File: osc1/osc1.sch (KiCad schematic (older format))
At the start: 48 parts

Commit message: Continued work on OSC1
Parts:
- added C?: 0.1u, symbol Device:C
- added C?: 10n, symbol Device:C
- added J?: Lin FM, symbol Connector:AudioJack2
- added R?: 1M, symbol Device:R
- added R?: 470, symbol Device:R
- added R? (x3): ?, symbol Device:R
- added RV? (x2): ?, symbol Device:R_POT
- R?: value 24k -> 100k
- RV?: value 10k -> 20k
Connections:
- net 1VOctave is gone; now on an unnamed net: R?.1
- net HIGHFREQTRACK is gone; now on net GND: RV?.3
- net +12V: now also R?.2, RV?.1, RV?.1
- net -12V: no longer J?.S
- net GND: now also J?.S, C?.1, J?.S, R?.1, R?.1
- net LINFM: now reaches U?.13 (VLFI)
- net LINFM: now also R?.1
- net at U?.15 (VFCI): now also RV?.2, R?.1, R?.1, RV?.2, RV?.2
- new net: C?.2, J?.T
- new net: C?.1, R?.2
- new net: C?.2, R?.2
- new net: R?.2, RV?.3 (x2)
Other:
- moved on the sheet: RV?

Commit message: Documentation and verifying hard+soft sync
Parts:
- removed J?: Tri, symbol Connector:AudioJack2
- removed J?: Saw, symbol Connector:AudioJack2
- removed J?: Pulse, symbol Connector:AudioJack2
- removed J?: 1V/Oct, symbol Connector:AudioJack2
- removed J?: HARDSYNC+, symbol Connector:AudioJack2
- removed J?: HARDSYNC-, symbol Connector:AudioJack2
- removed J?: Lin FM, symbol Connector:AudioJack2
- added J? (x2): AudioJack2_SwitchT, symbol Connector:AudioJack2_SwitchT
- added J?: Hard Sync +, symbol Connector:AudioJack2_SwitchT
- added J?: Hard Sync -, symbol Connector:AudioJack2_SwitchT
- added J?: Square Wave Output, symbol Connector:AudioJack2_SwitchT
- added J?: Saw Wave Output, symbol Connector:AudioJack2_SwitchT
- added J?: Triangular Wave Output, symbol Connector:AudioJack2_SwitchT
- added J?: Soft Sync Input, symbol Connector:AudioJack2_SwitchT
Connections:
- net GND: now also J?.S, J?.S, J?.S, J?.S, J?.S, J?.S, J?.S, J?.S, J?.TN, J?.TN, J?.TN, J?.TN
- net SOFTSYNC: now also C?.1, U?.9 (VSSI); no longer C?.2
- net at R?.1: now also J?.T (x3)
- net at R?.2: now also J?.T
- net at C?.2: now also J?.T (x3)
- new net: C?.2, J?.T
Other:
- note added: "# Status:\n\n## SoftSync\n\nJack is connected directly to CEM3340 input\nwith only a cap for DC protection (?). If no plug\nis inserted, the input is tied to ground.\n\n*Done!*\n\n## HardSync\n\nTwo jacks, hard sync positive and hard sync negative, are\nused as described in figure 4 of the CEM3340 datasheet.\nI’ve not dived into the details in how this works: I’ve just\ncopied the datasheet examp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"
- moved on the sheet: C?, D?, R?

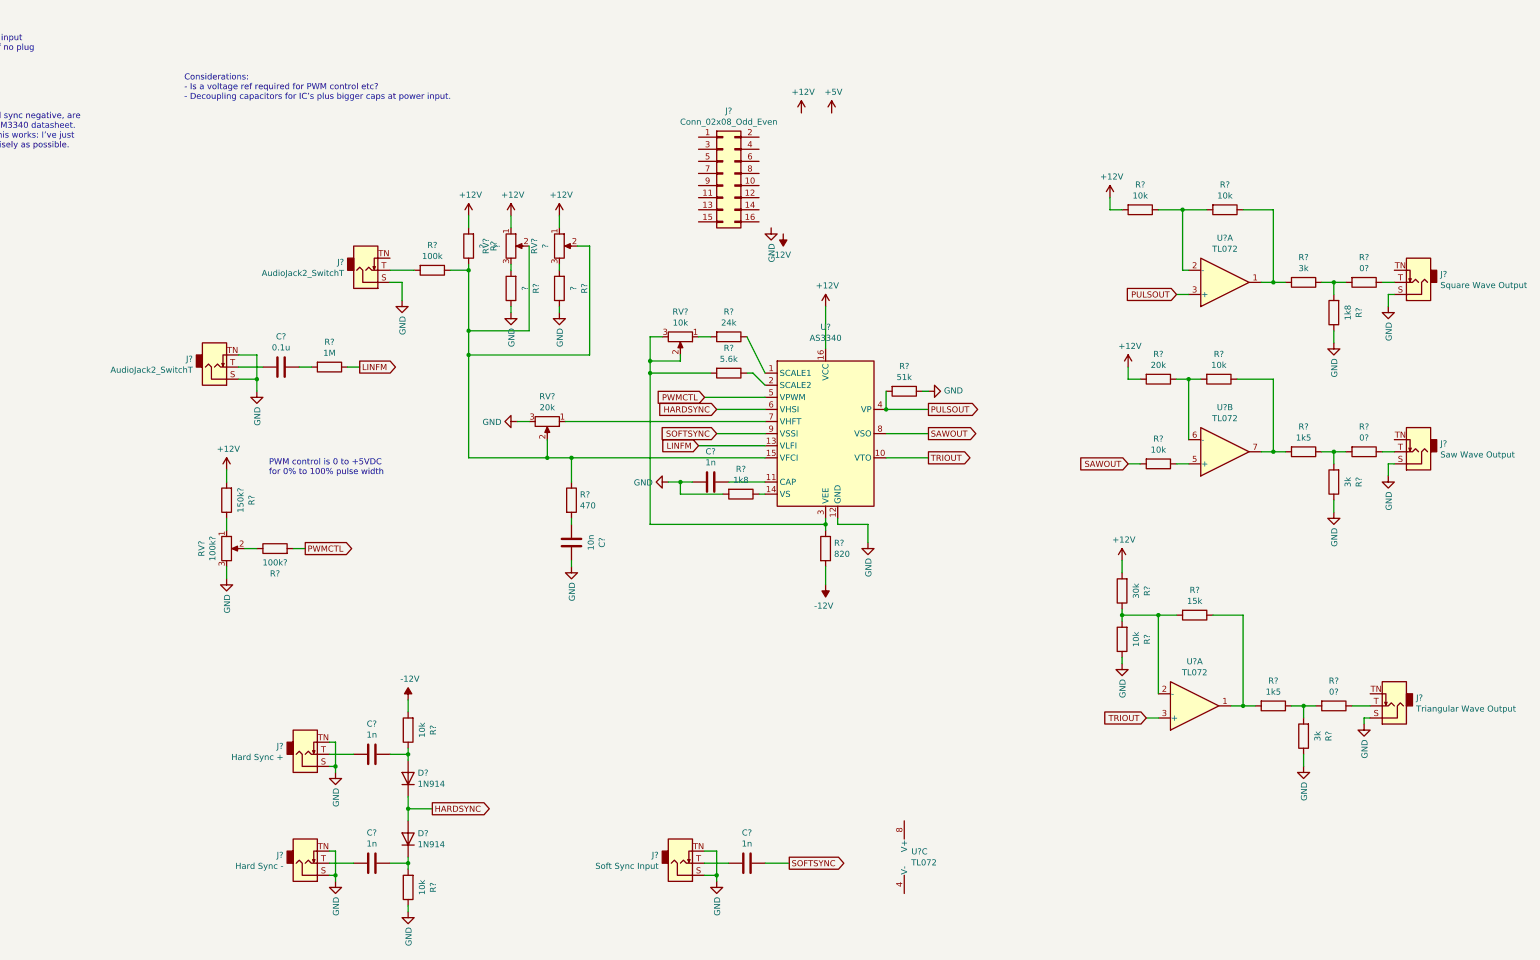
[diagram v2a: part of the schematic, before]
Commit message: Locked all pots and jacks
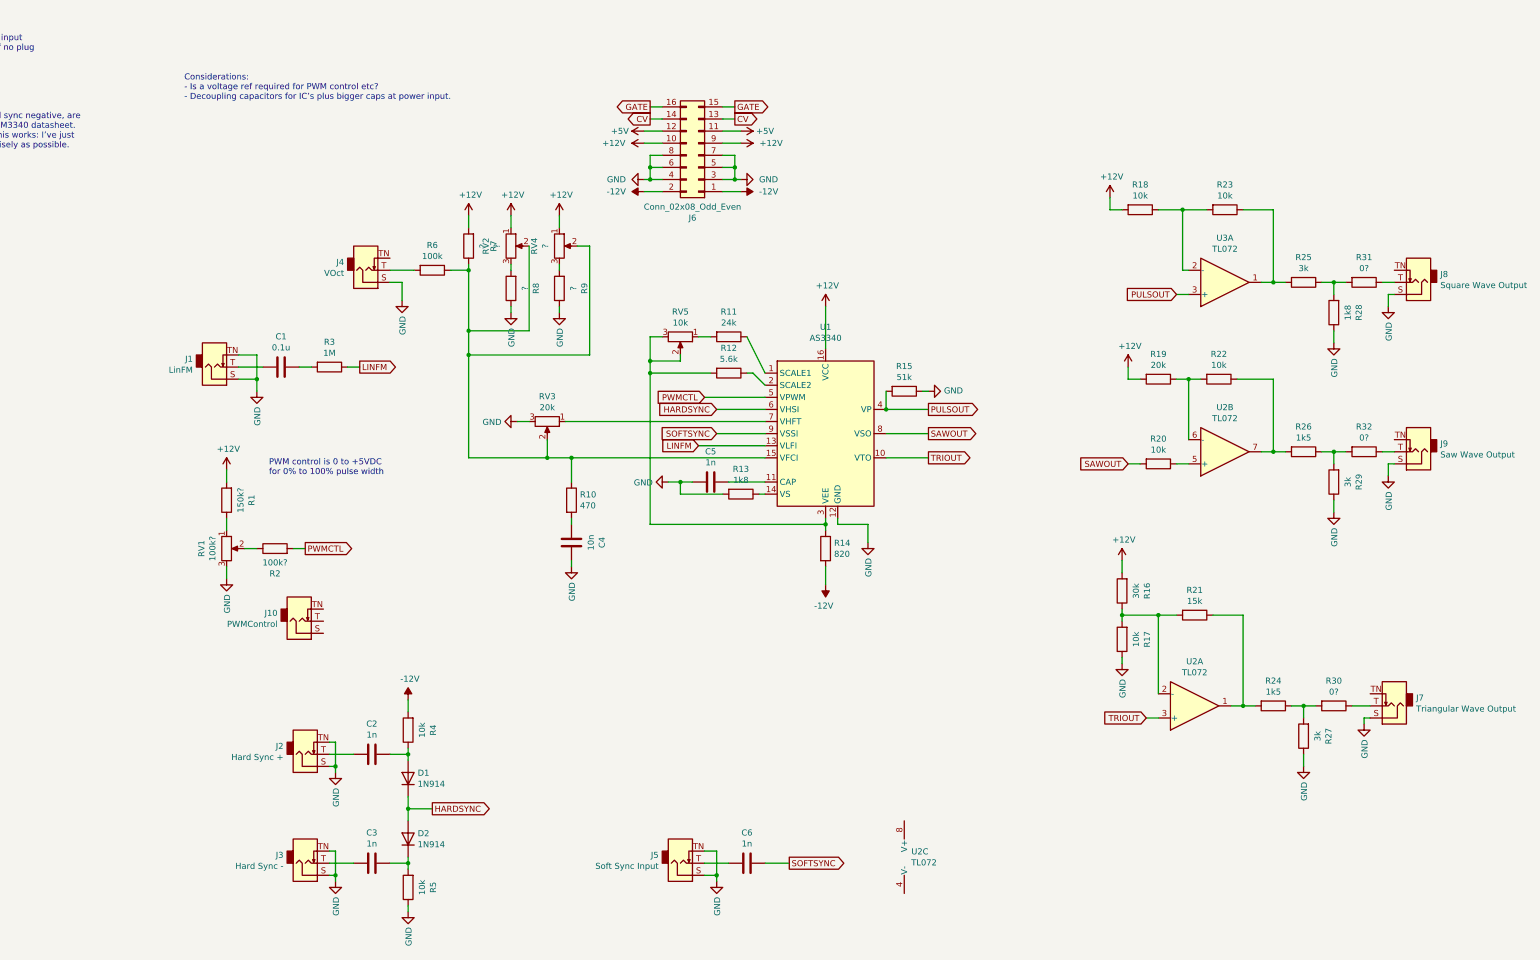
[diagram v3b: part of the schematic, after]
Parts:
- added J10: PWMControl, Connector_Audio:Jack_3.5mm_QingPu_WQP-PJ398SM_Vertical_CircularHoles, symbol Connector:AudioJack2_SwitchT
- C1, C2, C3, C4, C5, C6: renamed from C?; footprint (none) -> Capacitor_SMD:C_0603_1608Metric
- J1: renamed from J?; value AudioJack2_SwitchT -> LinFM; footprint (none) -> Connector_Audio:Jack_3.5mm_QingPu_WQP-PJ398SM_Vertical_CircularHoles
- J2, J3, J5, J7, J8, J9: renamed from J?; footprint (none) -> Connector_Audio:Jack_3.5mm_QingPu_WQP-PJ398SM_Vertical_CircularHoles
- J4: renamed from J?; value AudioJack2_SwitchT -> VOct; footprint (none) -> Connector_Audio:Jack_3.5mm_QingPu_WQP-PJ398SM_Vertical_CircularHoles
- J6: renamed from J?; footprint (none) -> Connector_IDC:IDC-Header_2x08_P2.54mm_Vertical
- R1, R10, R11, R12, R13, R14, R15, R16, R17, R18, R19, R2, R20, R21, R22, R23, R24, R25, R26, R27, R28, R29, R3, R30, R31, R32, R4, R5, R6, R7, R8, R9: renamed from R?; footprint (none) -> Resistor_SMD:R_0603_1608Metric
- RV1, RV2, RV4: renamed from RV?; footprint (none) -> Potentiometer_THT:Potentiometer_Alpha_RD901F-40-00D_Single_Vertical_CircularHoles
- RV3, RV5: renamed from RV?; footprint (none) -> Potentiometer_THT:Potentiometer_Bourns_3296W_Vertical
- U1: renamed from U?; footprint (none) -> Package_DIP:DIP-16_W7.62mm_Socket
- U2, U3: renamed from U?; footprint (none) -> Package_SO:SO-8_3.9x4.9mm_P1.27mm
- gave numbers to parts that had none: 2
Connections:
- net +12V: now also J6.10 (Pin_10), J6.9 (Pin_9)
- net +5V: now also J6.11 (Pin_11), J6.12 (Pin_12)
- net -12V: now also J6.1 (Pin_1), J6.2 (Pin_2)
- net GND: now also J6.3 (Pin_3), J6.4 (Pin_4), J6.5 (Pin_5), J6.6 (Pin_6), J6.7 (Pin_7), J6.8 (Pin_8)
- net CV: now reaches J6.13 (Pin_13)
- net CV: now also J6.14 (Pin_14)
- net GATE: now reaches J6.15 (Pin_15)
- net GATE: now also J6.16 (Pin_16)
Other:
- moved on the sheet: J6
